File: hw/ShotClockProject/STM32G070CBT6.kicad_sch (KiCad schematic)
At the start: 30 parts, among them J2 Conn_ST_STDC14, J3 Conn_01x06_Pin, SW1 SW_SPDT, U1 STM32F103RCT6, U2 LD39015M33R, Y1 16MHz

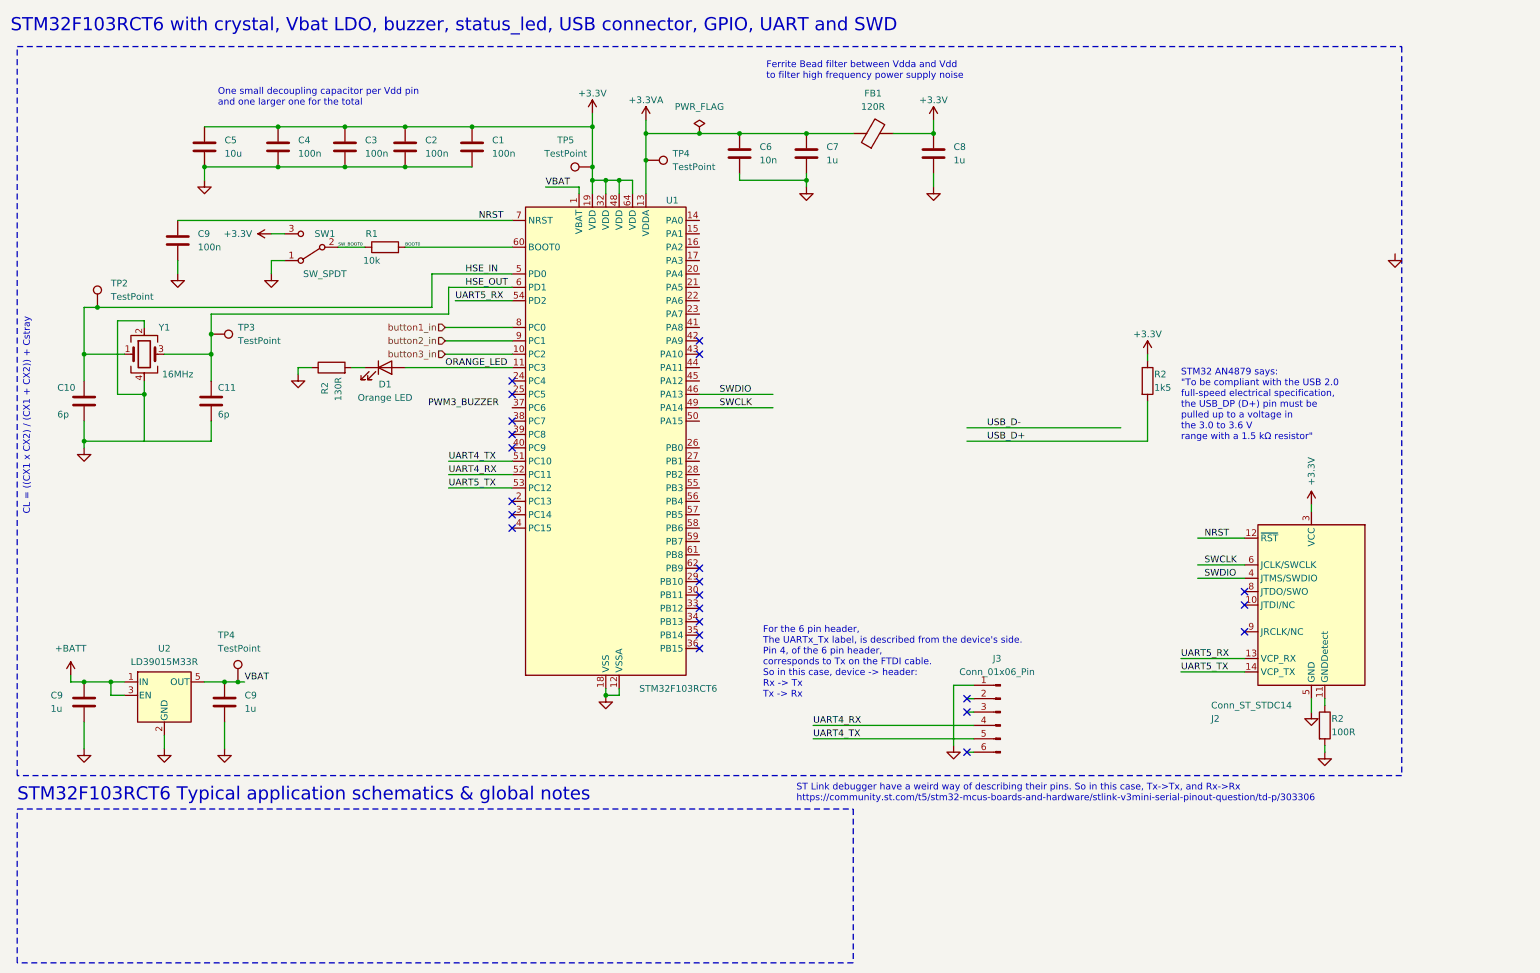
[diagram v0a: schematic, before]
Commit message: Started on integrating new STM32 MCU
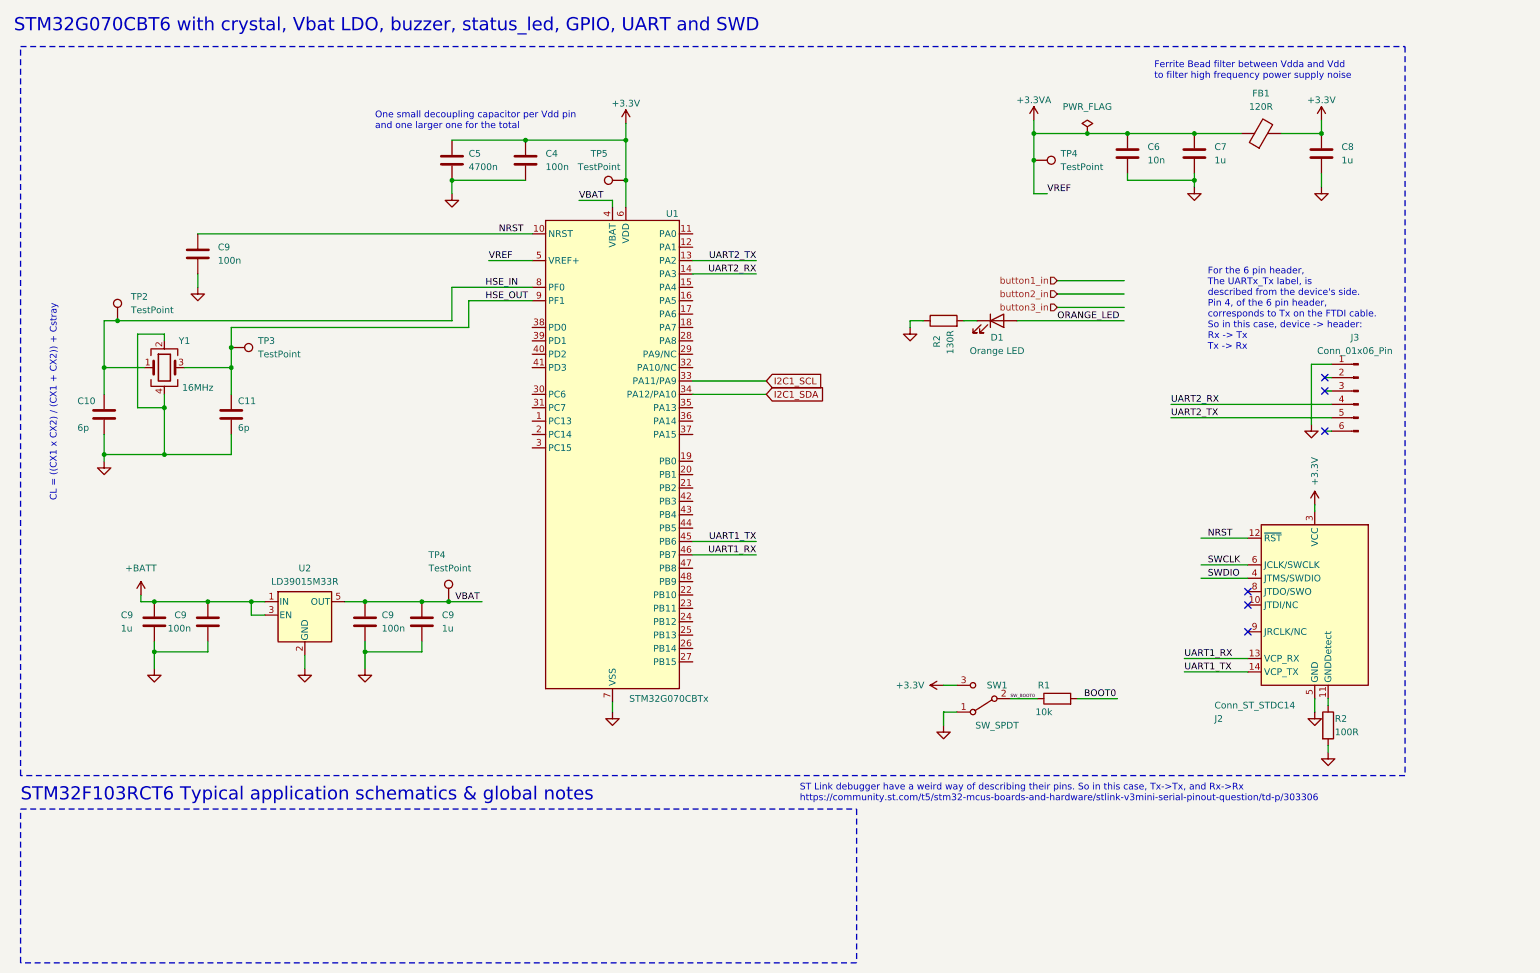
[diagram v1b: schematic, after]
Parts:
- removed C1, C2, C3, C9: 100n, Capacitor_SMD:C_0402_1005Metric, symbol Device:C
- removed C9 (x2): 1u, Capacitor_SMD:C_0402_1005Metric, symbol Device:C
- removed R2: 130R, Resistor_SMD:R_0402_1005Metric, symbol Device:R
- removed R2: 100R, Resistor_SMD:R_0402_1005Metric, symbol Device:R
- removed R2: 1k5, Resistor_SMD:R_0402_1005Metric, symbol Device:R
- removed TP4 (x2): TestPoint, TestPoint:TestPoint_Pad_D1.0mm, symbol Connector:TestPoint
- removed U1: STM32F103RCT6, Package_QFP:LQFP-64_10x10mm_P0.5mm, symbol MCU_ST_STM32F1:STM32F103RCTx
- added C9 (x3): 100n, Capacitor_SMD:C_0402_1005Metric, symbol Device:C
- added C9 (x2): 1u, Capacitor_SMD:C_0402_1005Metric, symbol Device:C
- added R2: 100R, Resistor_SMD:R_0402_1005Metric, symbol Device:R
- added R2: 130R, Resistor_SMD:R_0402_1005Metric, symbol Device:R
- added TP4 (x2): TestPoint, TestPoint:TestPoint_Pad_D1.0mm, symbol Connector:TestPoint
- added U1: STM32G070CBTx, Package_QFP:LQFP-48_7x7mm_P0.5mm, symbol MCU_ST_STM32G0:STM32G070CBTx
- C5: value 10u -> 4700n
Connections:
- net +3.3V: now also U1.6 (VDD)
- net +3.3VA: now also TP4.1, U1.5 (VREF+)
- net +BATT: now also C9.1, C9.1
- net GND: now also Y1.2, Y1.4, C9.2, C9.2, C9.2, C9.2, C9.2, R2.1, R2.2, U1.7 (VSS)
- net HSE_IN: now also U1.8 (PF0)
- net HSE_OUT: now also U1.9 (PF1)
- net NRST: now also C9.1, U1.10 (NRST)
- net VBAT: now also C9.1, C9.1, TP4.1, U1.4 (VBAT)
- net at D1.1 (K): now also R2.2
- net at J2.11 (GNDDetect): now also R2.1
- net UART4_RX renamed UART2_RX
- net UART2_RX: now also U1.14 (PA3)
- net UART4_TX renamed UART2_TX
- net UART2_TX: now also U1.13 (PA2)
- net UART5_RX renamed UART1_RX
- net UART1_RX: now also U1.46 (PB7)
- net UART5_TX renamed UART1_TX
- net UART1_TX: now also U1.45 (PB6)
- new net I2C1_SCL: U1.33 (PA11/PA9)
- new net I2C1_SDA: U1.34 (PA12/PA10)
- no-connect marks 23 -> 6
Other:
- note added: "STM32G070CBT6 with crystal, Vbat LDO, buzzer, status_led, GPIO, UART and SWD"
- note removed: "STM32 AN4879 says: "To be compliant with the USB 2.0 full-speed electrical specification, the USB_DP (D+) pin must be pulled up to a voltage in the 3.0 to 3.6 V range with a 1.5 kΩ resistor""
- note removed: "STM32F103RCT6 with crystal, Vbat LDO, buzzer, status_led, USB connector, GPIO, UART and SWD"
- title: Shotclock Mainboard -> (none)

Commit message: Added I2C support
Calculated pull-up resistor values
Added 6 pin female headers to mainboard
Added nRESET line for the I2C chips
Removed PCB routing and part placement
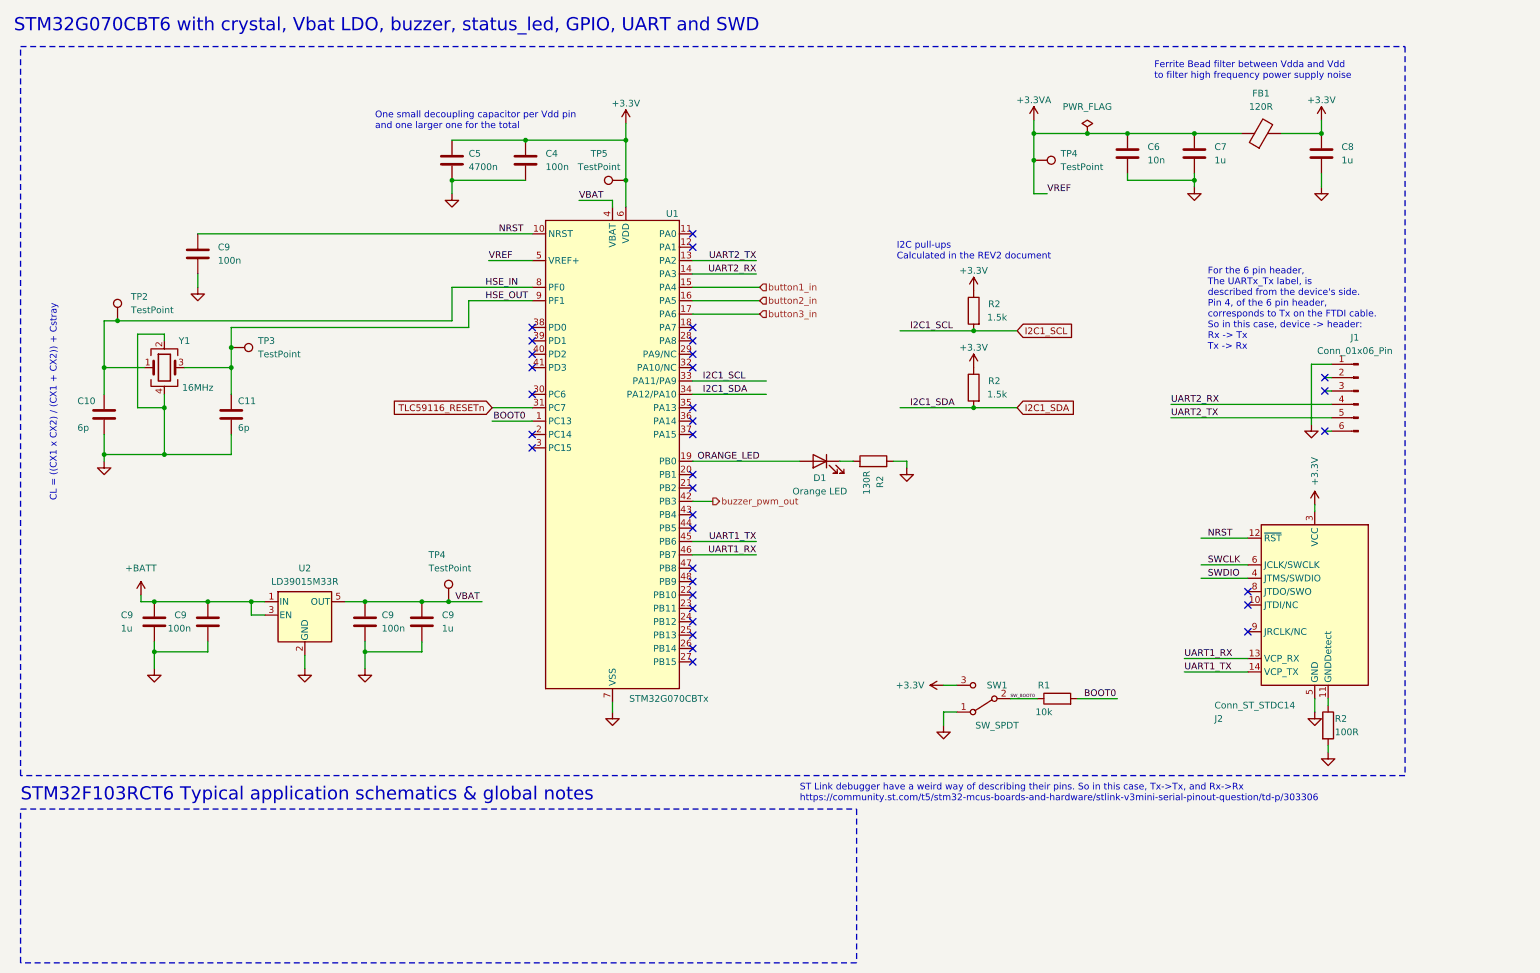
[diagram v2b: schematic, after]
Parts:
- added R2 (x2): 1.5k, Resistor_SMD:R_0402_1005Metric, symbol Device:R
- renumbered J3 to J1
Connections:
- net +3.3V: now also R2.1, R2.1
- net BOOT0: now also U1.1 (PC13)
- net I2C1_SCL: now also R2.2
- net I2C1_SDA: now also R2.2
- net ORANGE_LED: now also U1.19 (PB0)
- net button1_in: now also U1.15 (PA4)
- net button2_in: now also U1.16 (PA5)
- net button3_in: now also U1.17 (PA6)
- net TLC59116_RESETn: now reaches U1.31 (PC7)
- net buzzer_pwm_out: now reaches U1.42 (PB3)
- no-connect marks 6 -> 34
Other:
- note added: "I2C pull-ups Calculated in the REV2 document"
- moved on the sheet: D1, R2

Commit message: XTAL, decoup placement & I2C routing
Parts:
- C5: footprint Capacitor_SMD:C_0603_1608Metric -> Capacitor_SMD:C_0402_1005Metric
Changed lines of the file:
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@@
       (effects (font (size 1.27 1.27)) (justify left))
     )
-    (property "Footprint" "Capacitor_SMD:C_0603_1608Metric" (at 98.7552 46.99 0)
+    (property "Footprint" "Capacitor_SMD:C_0402_1005Metric" (at 98.7552 46.99 0)
       (effects (font (size 1.27 1.27)) hide)
     )
